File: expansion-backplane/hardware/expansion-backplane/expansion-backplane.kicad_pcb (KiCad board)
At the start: 2 copper layers, 100 x 51 mm, 15 parts, among them J1 Barrel_Jack, SW1 SW_SPDT

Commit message: updatedd PCB layouts
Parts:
- moved SW1 3.66 mm to (106.9, 135.7)
- moved C2 2.51 mm to (135.0, 137.7)
- moved C3 2.51 mm to (153.0, 137.7)
- moved C4 2.51 mm to (171.0, 137.7)
- moved C5 2.51 mm to (189.0, 137.7)
- moved CN2 2.51 mm to (132.9, 131.0)
- moved CN3 2.51 mm to (150.9, 131.0)
- moved CN4 2.51 mm to (168.9, 131.0)
- moved CN5 2.51 mm to (186.9, 131.0)
- moved C1 2.51 mm to (117.0, 137.7)
- moved CN1 2.51 mm to (115.0, 131.0)
- moved R1 1.78 mm to (109.0, 114.3)
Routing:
- net BUS6: track 0.00 -> 76.1 mm
- net BUS2: track 0.00 -> 76.1 mm
- net A8: track 0.00 -> 76.1 mm
- net A6: track 0.00 -> 76.1 mm
- net ~{RESET}: track 0.00 -> 76.0 mm
- net A2: track 0.00 -> 76.0 mm
- net ~{RO}: track 0.00 -> 76.0 mm
- net INH: track 0.00 -> 76.0 mm
- net A12: track 0.00 -> 76.0 mm
- net BUS4: track 0.00 -> 76.0 mm
- net BUS0: track 0.00 -> 76.0 mm
- net A4: track 0.00 -> 76.0 mm
- net A14: track 0.00 -> 76.0 mm
- net A10: track 0.00 -> 76.0 mm
- net A0: track 0.00 -> 76.0 mm
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- added copper zone on B.Cu, net GND
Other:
- board text added: "+5V"
- board text added: "A0"
- board text added: "A1"
- board text added: "A10"
- board text added: "A11"
- board text added: "A12"
- board text added: "A13"
- board text added: "A14"
- board text added: "A15"
- board text added: "A2"
- board text added: "A3"
- board text added: "A4"
- board text added: "A5"
- board text added: "A6"
- board text added: "A7"
- board text added: "A8"
- board text added: "A9"
- board text added: "BUS0"
- board text added: "BUS1"
- board text added: "BUS2"
- board text added: "BUS3"
- board text added: "BUS4"
- board text added: "BUS5"
- board text added: "BUS6"
- board text added: "BUS7"
- board text added: "CLK"
- board text added: "GND"
- board text added: "INH"
- board text added: "Minimal 64x4 Expansion Backplane"
- board text added: "NC/USER"
- board text added: "v1.0 by Michael Kamprath"
- board text added: "~{RESET}"
- board text added: "~{RI}"
- board text added: "~{RO}"

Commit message: update speech pld file and more
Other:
- board text added: "To Back -->"
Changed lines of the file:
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@@
 			(outputformat 1)
 			(mirror no)
-			(drillshape 1)
+			(drillshape 0)
 			(scaleselection 1)
-			(outputdirectory "")
+			(outputdirectory "gerbers_v1")
 		)
 	)
@@
 		)
 	)
+	(gr_text "To Back -->"
+		(at 124.968 99.822 90)
+		(layer "F.SilkS")
+		(effects
+			(font
+				(size 0.8 0.8)
+				(thickness 0.1)
+			)
+			(justify left bottom)
+		)
+	)

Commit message: improved backplane
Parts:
- added C4: 0.1 uF, Capacitor_THT:C_Disc_D3.8mm_W2.6mm_P2.50mm, F.Cu at (179.1, 133.3)
- added REF**: MountingHole_2.2mm_M2, MountingHole:MountingHole_2.2mm_M2, F.Cu at (97.4, 138.5)
- added REF**: MountingHole_2.2mm_M2, MountingHole:MountingHole_2.2mm_M2, F.Cu at (211.6, 92.5)
- added REF**: MountingHole_2.2mm_M2, MountingHole:MountingHole_2.2mm_M2, F.Cu at (97.4, 92.5)
- added REF**: MountingHole_2.2mm_M2, MountingHole:MountingHole_2.2mm_M2, F.Cu at (211.6, 138.5)
- added U1: 74LS126, Package_DIP:DIP-14_W7.62mm, F.Cu at (182.6, 138.7)
- moved C7 17.5 mm to (206.5, 137.7)
- moved CN5 17.3 mm to (204.2, 131.0)
- moved D1 5.51 mm to (99.8, 131.6)
- moved C3 2.25 mm to (137.2, 137.7)
- moved C5 2.25 mm to (155.2, 137.7)
- moved C6 2.25 mm to (173.2, 137.7)
- moved CN2 2.25 mm to (135.1, 131.0)
- moved CN3 2.25 mm to (153.1, 131.0)
- moved CN4 2.25 mm to (171.1, 131.0)
- moved R1 2.25 mm to (111.2, 114.3)
- moved C1 2.25 mm to (119.2, 137.7)
- moved C2 2.25 mm to (105.1, 111.8)
- moved CN1 2.25 mm to (117.2, 131.0)
- moved J1 2.25 mm to (104.9, 104.0)
- moved SW1 2.25 mm to (109.2, 135.7)
- renumbered C6 to C2, C2 to C3, C3 to C5, C4 to C6, C5 to C7
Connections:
- CN1 pad 3: INH -> Net-(CN1-INH)
- CN2 pad 3: INH -> Net-(CN2-INH)
- CN3 pad 3: INH -> Net-(CN3-INH)
- CN4 pad 3: INH -> Net-(CN4-INH)
- CN5 pad 3: INH -> Net-(CN5-INH)
- CN5 pad 4: USER -> unconnected-(CN5-NC-Pad4)
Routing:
- net INH: track 76.0 -> 0.00 mm
- net Net-(CN1-INH): track 0.00 -> 69.6 mm
- net Net-(CN2-INH): track 0.00 -> 59.3 mm
- net +5V: track 149.0 -> 196.5 mm
- net Net-(CN3-INH): track 0.00 -> 43.7 mm
- net Net-(CN5-INH): track 0.00 -> 40.0 mm
- net GND: track 160.9 -> 185.5 mm
- net USER: track 75.8 -> 56.8 mm
- net A11: track 75.8 -> 91.6 mm
- net A9: track 75.8 -> 91.4 mm
- net A5: track 75.8 -> 91.3 mm
- net A15: track 75.8 -> 91.3 mm
- net CLK: track 75.8 -> 91.2 mm
- net BUS3: track 75.8 -> 91.2 mm
- net ~{RI}: track 75.8 -> 91.1 mm
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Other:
- board size 100 x 51 mm -> 119 x 51 mm
- board text added: "74AHCT126"
- board text added: "connector to Minimal 64x4"
- board text added: "v1.1 by Michael Kamprath"
- board text removed: "v1.0 by Michael Kamprath"

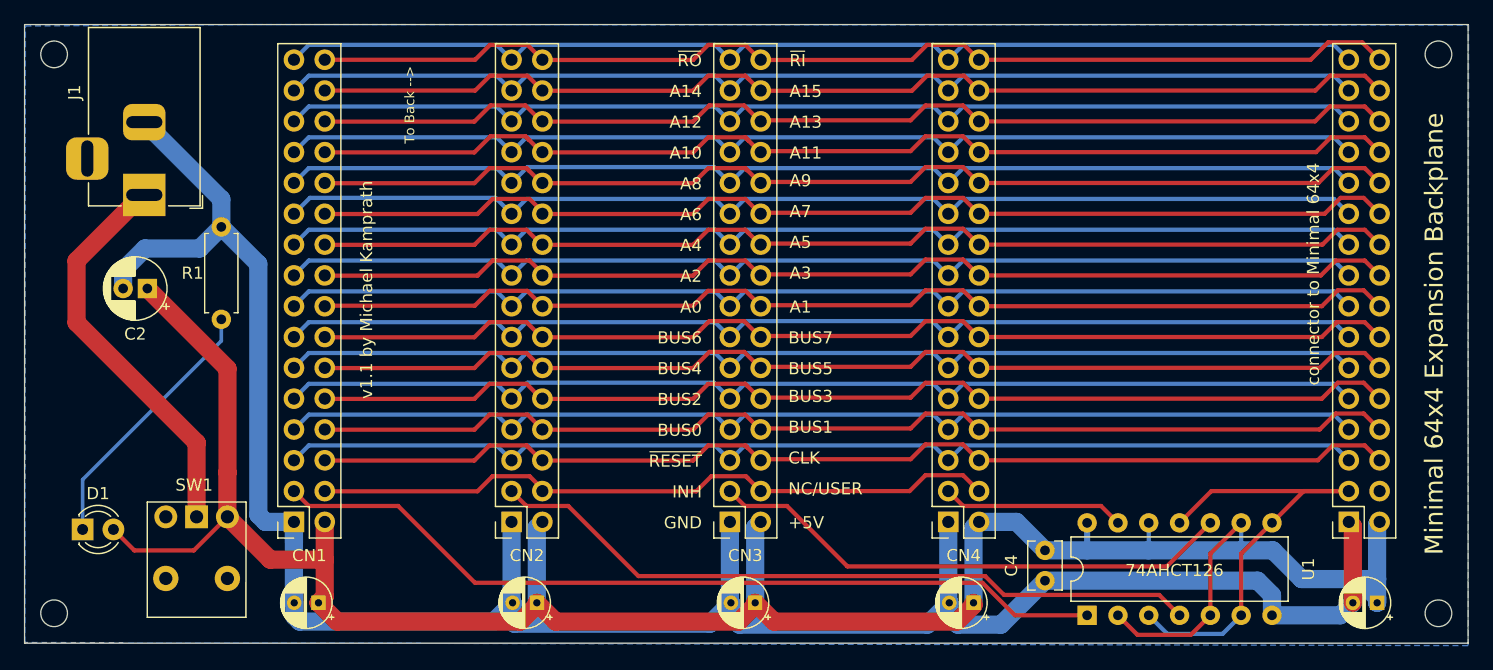
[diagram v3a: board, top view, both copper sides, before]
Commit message: added pull down resistors
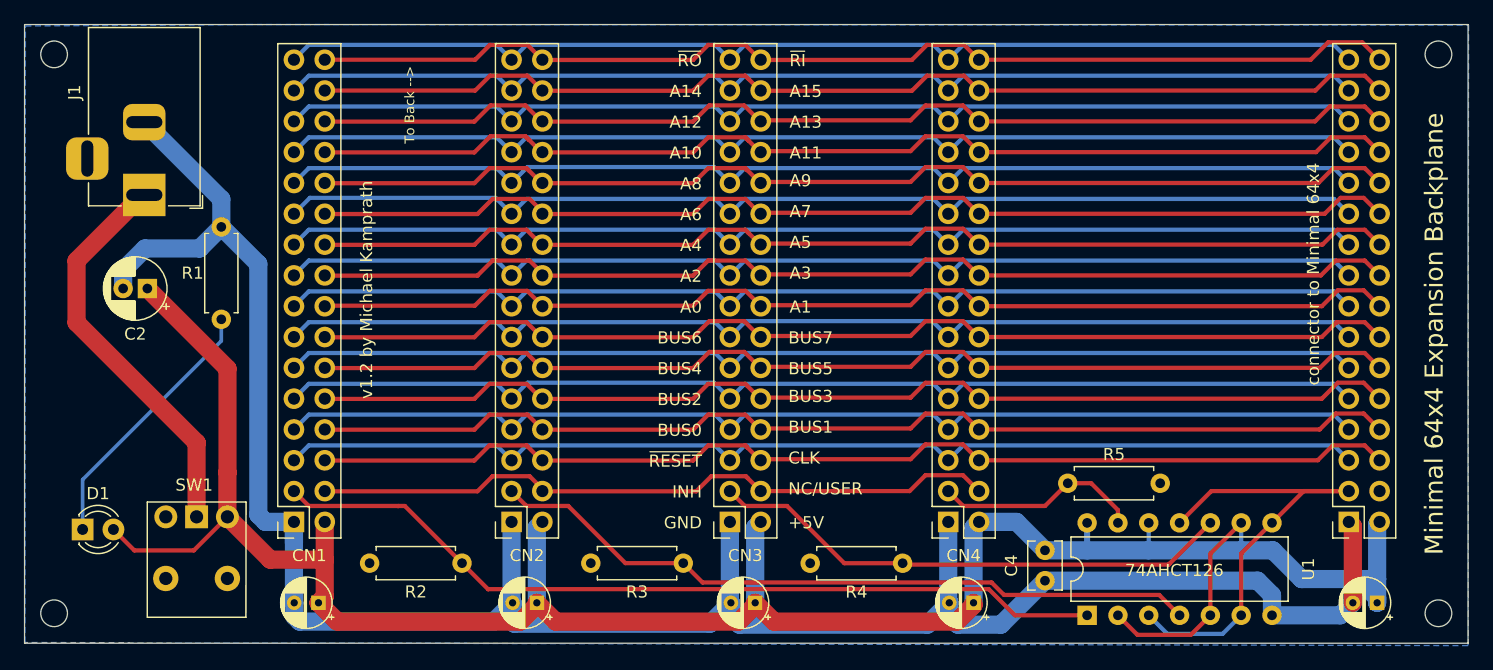
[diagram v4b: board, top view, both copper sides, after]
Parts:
- added R2: 10K, Resistor_THT:R_Axial_DIN0207_L6.3mm_D2.5mm_P7.62mm_Horizontal, F.Cu at (131.1, 134.4)
- added R3: 10K, Resistor_THT:R_Axial_DIN0207_L6.3mm_D2.5mm_P7.62mm_Horizontal, F.Cu at (149.3, 134.4)
- added R4: 10K, Resistor_THT:R_Axial_DIN0207_L6.3mm_D2.5mm_P7.62mm_Horizontal, F.Cu at (167.4, 134.4)
- added R5: 10K, Resistor_THT:R_Axial_DIN0207_L6.3mm_D2.5mm_P7.62mm_Horizontal, F.Cu at (181.0, 127.8)
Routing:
- net Net-(CN4-INH): track 15.1 -> 17.2 mm
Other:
- board text added: "v1.2 by Michael Kamprath"
- board text removed: "v1.1 by Michael Kamprath"

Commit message: added pull down resistor
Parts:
- added R6: 1K, Resistor_THT:R_Axial_DIN0207_L6.3mm_D2.5mm_P7.62mm_Horizontal, F.Cu at (190.7, 127.8)
- U1: value 74LS126 -> 74AHCT126
- moved R5 1.93 mm to (179.1, 127.8)
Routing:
- net Net-(CN5-INH): track 40.0 -> 37.0 mm
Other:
- board text added: "10K"
- board text added: "1K"
- board text added: "330"
